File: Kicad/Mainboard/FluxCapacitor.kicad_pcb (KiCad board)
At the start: 2 copper layers, 100 x 100 mm, 99 parts, among them J1 PJ-002A, J2 TM_1, J3 TM_2, J7 TM_4, J8 TM_2, J9 RELAY, M1 SYS_FAN, Q2 IRF4905PBF, Q3 2N7000, Q4 2N7000, U1 OKI-78SR-5_1.5-W36-C, U2 ESP32_DEVBOARD, U4 HT16K33_DEVBOARD, U5 PCA9306DCUR

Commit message: Continued mainboard layout
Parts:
- moved R16 197.6 mm to (274.0, 111.5)
- moved TP23 191.6 mm to (281.5, 24.5)
- moved TP17 188.4 mm to (276.0, 46.5)
- moved C14 188.2 mm to (241.2, 143.0)
- moved C15 188.2 mm to (236.0, 143.3)
- moved C16 188.2 mm to (235.5, 150.5)
- moved C19 188.2 mm to (284.3, 51.9)
- moved C20 188.2 mm to (253.4, 105.5)
- moved C21 188.2 mm to (284.3, 55.0)
- moved C5 188.2 mm to (284.3, 39.9)
- moved C6 188.2 mm to (284.3, 42.9)
- moved C7 188.2 mm to (284.3, 45.9)
- moved D10 188.2 mm to (257.5, 39.9)
- moved D11 188.2 mm to (257.5, 43.0)
- moved D12 188.2 mm to (257.5, 46.0)
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
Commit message: Finished Mainboard Layout
-Now all that needs to be done is to resolve all DRC errors
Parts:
- TP15, TP16, TP17, TP18, TP19, TP20, TP21, TP22, TP23, TP24, TP25, TP6, TP7: footprint FluxCapacitor:TestPoint_Pad_D2.0mm -> FluxCapacitor:TestPoint_Pad_D1.5mm
- moved C19 194.9 mm to (94.0, 94.0), turned to -90 degrees
- moved Q3 186.8 mm to (95.2, 119.2), turned to 90 degrees
- moved TP23 181.5 mm to (121.0, 109.2)
- moved TP3 177.4 mm to (95.5, 61.8), turned to -90 degrees
- moved TP24 174.1 mm to (116.0, 109.2)
- moved R29 170.7 mm to (99.2, 118.0)
- moved R30 170.4 mm to (99.5, 121.0)
- moved TP22 170.1 mm to (123.5, 109.2)
- moved TP21 169.4 mm to (126.0, 109.2)
- moved TP20 168.9 mm to (128.5, 109.2)
- moved TP25 161.1 mm to (133.5, 121.8), turned to 180 degrees
- moved TP19 154.8 mm to (131.0, 109.2)
- moved TP18 154.0 mm to (133.5, 109.2)
- moved C6 152.5 mm to (146.2, 107.5), turned to 180 degrees
- moved C7 132.5 mm to (175.8, 121.8), turned to 180 degrees
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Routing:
- net +3V3: track 0.00 -> 270.6 mm, vias 0 -> 11
- net 5V_RAW: track 0.00 -> 177.3 mm, vias 0 -> 8
- net /I2C_SCL: track 0.00 -> 146.9 mm, vias 0 -> 9
- net /I2C_SDA: track 0.00 -> 143.2 mm, vias 0 -> 8
- net 12V_PROTECTED: track 0.00 -> 134.5 mm, vias 0 -> 10
- net /HALL_1: track 0.00 -> 114.7 mm, vias 0 -> 4
- net /HALL_3: track 0.00 -> 112.2 mm, vias 0 -> 1
- net /HALL_2: track 0.00 -> 101.4 mm
- net Net-(U2-P25): track 0.00 -> 98.8 mm, vias 0 -> 5
- net Net-(U2-P27): track 0.00 -> 89.1 mm, vias 0 -> 1
- net /HALL_4: track 0.00 -> 86.6 mm
- net /12V_RAW: track 0.00 -> 83.0 mm, vias 0 -> 5
- net /M3_PRESET_LED_2: track 0.00 -> 81.3 mm, vias 0 -> 2
- net /BUZZER_DRV: track 0.00 -> 80.9 mm, vias 0 -> 2
- net /MAIN_POWER_SENSE: track 0.00 -> 80.4 mm, vias 0 -> 1
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- added copper zone on B.Cu, net GND
- added copper zone on F.Cu, net GND

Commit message: Finished Mainboard PCB
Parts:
- added REF**: MountingHole_3.2mm_M3, MountingHole:MountingHole_3.2mm_M3, F.Cu at (129.6, 103.2)
- moved TP24 2.30 mm to (118.3, 109.2)
- moved TP6 1.55 mm to (189.1, 55.8), turned to -90 degrees
- moved TP7 1.30 mm to (189.1, 58.3), turned to 180 degrees
- moved R5 1.20 mm to (188.9, 52.6), turned to 90 degrees
- moved D10 0.75 mm to (167.8, 101.5)
- moved D11 0.75 mm to (171.2, 101.5)
- moved D12 0.75 mm to (174.8, 101.5)
- moved D16 0.75 mm to (189.8, 101.5)
- moved D17 0.75 mm to (186.2, 101.5)
- moved D18 0.75 mm to (182.8, 101.5)
- moved D19 0.75 mm to (179.2, 101.5)
- moved D8 0.75 mm to (160.8, 101.5)
- moved D9 0.75 mm to (164.2, 101.5)
- moved R7 0.75 mm to (190.5, 75.0)
- moved R32 0.50 mm to (160.0, 46.8)
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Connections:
- U4 pad 19: /FAULT LEDS/A1 -> unconnected-(U4-A15-Pad19)
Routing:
- net +3V3: track 270.6 -> 289.9 mm, vias 11 -> 15
- net /BTN_EXP_INT: track 75.5 -> 87.5 mm, vias 5 -> 6
- net /I2C_SCL: track 146.9 -> 153.2 mm
- net /12V_RAW: track 83.0 -> 88.7 mm, vias 5 -> 8
- net /FAULT LEDS/A6: track 51.4 -> 57.0 mm, vias 2 -> 5
- net Net-(U2-P27): track 89.1 -> 94.4 mm, vias 1 -> 5
- net Net-(U2-P14): track 71.7 -> 75.4 mm
- net Net-(U2-P26): track 76.7 -> 79.6 mm
- net Net-(U2-P25): track 98.8 -> 101.4 mm, vias 5 -> 7
- net /FAULT LEDS/A1: track 43.4 -> 45.6 mm
- net Net-(D2-K): track 28.6 -> 30.5 mm
- net Net-(U_BTN_EXPANDER1-GPA7): track 2.48 -> 3.76 mm
- net Net-(D9-A): track 2.97 -> 2.22 mm
- net Net-(D8-A): track 2.97 -> 2.22 mm
- net Net-(D19-A): track 2.98 -> 2.23 mm
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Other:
- outline, holes or cut-outs redrawn
- board text added: "12V_PRO"
- board text added: "12V_RAW"
- board text added: "3V3"
- board text added: "5V_RAW"
- board text added: "5V_SYS"
- board text added: "DBG1"
- board text added: "DBG2"
- board text added: "DBG3"
- board text added: "DBG4"
- board text added: "DEBUG LEDS"

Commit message: Added a little mark showing it was my work
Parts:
- added G***: LOGO, FluxCapacitor:FluxCapacitorImage, B.Cu at (175.2, 55.0)
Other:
- board text added: "FLUX CAPACITOR MAINBOARD"
- board text added: "FOR HEELUXE"
- board text added: "MADE BY JOSHUA SMALL"
- board text added: "REV 0 - JULY 2026"

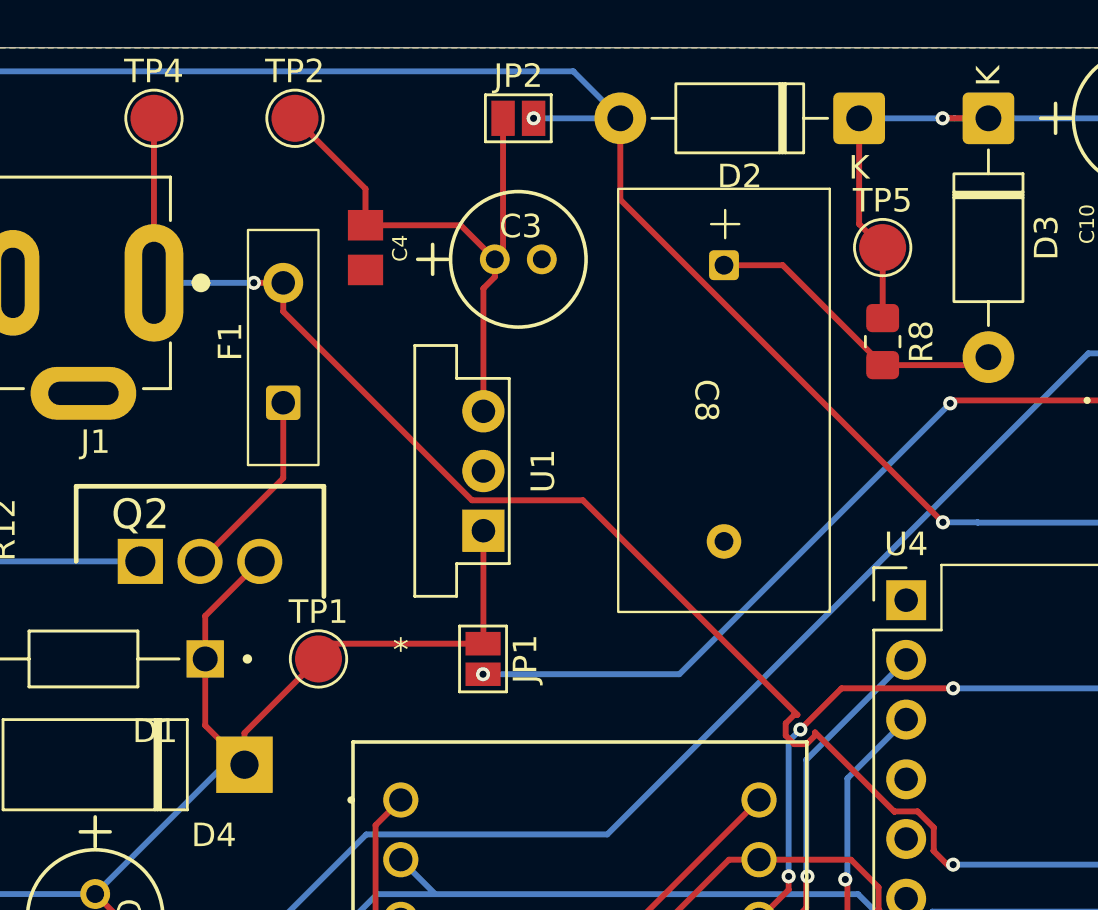
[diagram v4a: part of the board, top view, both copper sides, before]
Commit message: Made relay splitter daughterboard
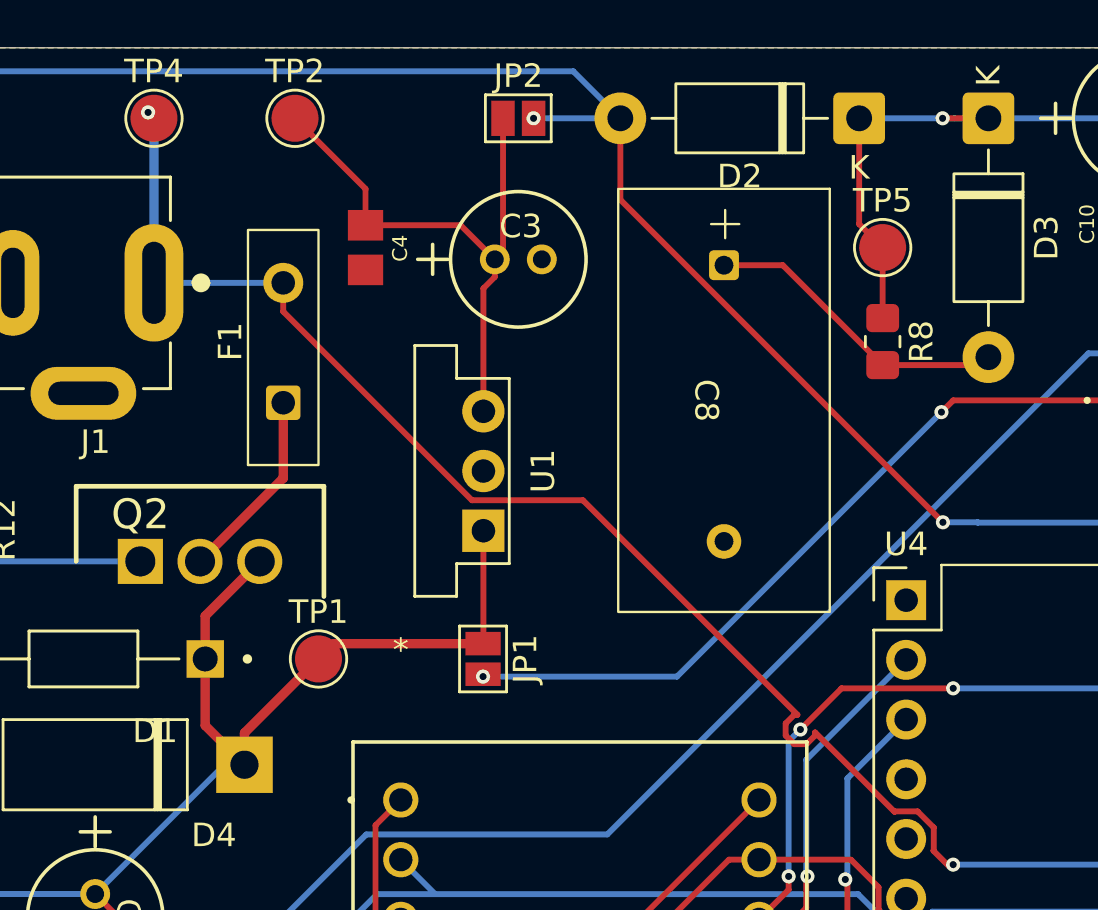
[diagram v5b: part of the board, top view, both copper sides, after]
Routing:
- net /12V_RAW: track 88.7 -> 89.4 mm, vias 8 -> 7
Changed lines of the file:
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@@
 	)
 	(segment
-		(start 112.75 70.75)
-		(end 113.4 70.1)
-		(width 0.25)
+		(start 113.4 70.1)
+		(end 119.75 70.1)
+		(width 0.4)
 		(layer "F.Cu")
 		(net "Net-(D4-K)")
 	)
 	(segment
-		(start 109.6 75.25)
-		(end 109.6 73.9)
+		(start 119.75 70)
+		(end 119.765 69.985)
 		(width 0.25)
 		(layer "F.Cu")
@@
 	)
 	(segment
-		(start 107.93 68.92)
-		(end 110.25 66.6)
+		(start 119.75 70.1)
+		(end 119.75 70)
 		(width 0.25)
 		(layer "F.Cu")
@@
 	)
 	(segment
-		(start 119.75 70)
-		(end 119.765 69.985)
-		(width 0.25)
+		(start 109.6 73.9)
+		(end 112.75 70.75)
+		(width 0.4)
 		(layer "F.Cu")
 		(net "Net-(D4-K)")
 	)
 	(segment
-		(start 119.75 70.1)
-		(end 119.75 70)
-		(width 0.25)
+		(start 107.93 73.58)
+		(end 109.6 75.25)
+		(width 0.4)
 		(layer "F.Cu")
 		(net "Net-(D4-K)")
@@
 	)
 	(segment
-		(start 105.25 82.75)
-		(end 105.25 85.75)
-		(width 0.25)
+		(start 110.25 66.6)
+		(end 107.93 68.92)
+		(width 0.4)
 		(layer "F.Cu")
 		(net "Net-(D4-K)")
 	)
 	(segment
-		(start 107.93 70.75)
-		(end 107.93 68.92)
+		(start 105.25 82.75)
+		(end 105.25 85.75)
 		(width 0.25)
 		(layer "F.Cu")
@@
 	)
 	(segment
-		(start 107.93 73.58)
-		(end 109.6 75.25)
-		(width 0.25)
+		(start 109.6 75.25)
+		(end 109.6 73.9)
+		(width 0.4)
 		(layer "F.Cu")
 		(net "Net-(D4-K)")
 	)
 	(segment
-		(start 109.6 73.9)
-		(end 112.75 70.75)
-		(width 0.25)
+		(start 107.93 68.92)
+		(end 107.93 70.75)
+		(width 0.4)
 		(layer "F.Cu")
 		(net "Net-(D4-K)")
@@
 		(start 107.93 70.75)
 		(end 107.93 73.58)
-		(width 0.25)
+		(width 0.4)
 		(layer "F.Cu")
 		(net "Net-(D4-K)")
 	)
 	(segment
-		(start 113.4 70.1)
-		(end 119.75 70.1)
-		(width 0.25)
+		(start 112.75 70.75)
+		(end 113.4 70.1)
+		(width 0.4)
 		(layer "F.Cu")
 		(net "Net-(D4-K)")
@@
 	)
 	(segment
+		(start 109.6 75.25)
+		(end 108.75 75.25)
+		(width 0.25)
+		(layer "B.Cu")
+		(net "Net-(D4-K)")
+	)
+	(segment
 		(start 108.75 75.25)
 		(end 103.25 80.75)
@@
 	)
 	(segment
-		(start 109.6 75.25)
-		(end 108.75 75.25)
-		(width 0.25)
-		(layer "B.Cu")
-		(net "Net-(D4-K)")
-	)
-	(segment
 		(start 188.25 122.75)
 		(end 188.25 123.805)
@@
 	)
 	(segment
+		(start 139.25 60.25)
+		(end 139.75 59.75)
+		(width 0.25)
+		(layer "F.Cu")
+		(net "12V_PROTECTED")
+	)
+	(segment
 		(start 168.365 112.095991)
 		(end 170.905 114.635991)
@@
 	)
 	(segment
-		(start 139.75 59.75)
-		(end 146.9459 59.75)
-		(width 0.25)
-		(layer "F.Cu")
-		(net "12V_PROTECTED")
-	)
-	(segment
 		(start 167.824476 110.668076)
 		(end 168.365 111.2086)
@@
 	)
 	(segment
-		(start 139.625 59.875)
-		(end 139.75 59.75)
+		(start 139.75 59.75)
+		(end 146.9459 59.75)
 		(width 0.25)
 		(layer "F.Cu")
@@
 	)
 	(via
-		(at 139.625 59.875)
+		(at 139.25 60.25)
 		(size 0.6)
 		(drill 0.3)
@@
 	)
 	(via
-		(at 119.75 71.4)
+		(at 119.75 71.5)
 		(size 0.6)
 		(drill 0.3)
@@
 	)
 	(segment
-		(start 139.625 59.875)
-		(end 128.1 71.4)
-		(width 0.25)
-		(layer "B.Cu")
-		(net "12V_PROTECTED")
-	)
-	(segment
 		(start 165.271092 91.75)
 		(end 165.271092 91.521092)
@@
 	)
 	(segment
-		(start 128.1 71.4)
-		(end 119.75 71.4)
-		(width 0.25)
-		(layer "B.Cu")
-		(net "12V_PROTECTED")
-	)
-	(segment
 		(start 167.824476 110.668076)
 		(end 167.0214 109.865)
@@
 	)
 	(segment
+		(start 139.25 60.25)
+		(end 128 71.5)
+		(width 0.25)
+		(layer "B.Cu")
+		(net "12V_PROTECTED")
+	)
+	(segment
+		(start 128 71.5)
+		(end 119.75 71.5)
+		(width 0.25)
+		(layer "B.Cu")
+		(net "12V_PROTECTED")
+	)
+	(segment
 		(start 180.345 127.9)
 		(end 180.3 127.9)
@@
 	)
 	(segment
+		(start 105.75 47.75)
+		(end 105.5 47.5)
+		(width 0.4)
+		(layer "F.Cu")
+		(net "/12V_RAW")
+	)
+	(segment
 		(start 138.91085 78.91085)
 		(end 139.585 79.585)
@@
 	)
 	(segment
-		(start 105.75 47.75)
-		(end 105.75 54.75)
-		(width 0.25)
-		(layer "F.Cu")
-		(net "/12V_RAW")
-	)
-	(segment
 		(start 137.249149 77.249149)
 		(end 137.263299 77.235)
@@
 	)
 	(segment
-		(start 110 54.75)
-		(end 111.25 54.75)
-		(width 0.25)
-		(layer "F.Cu")
-		(net "/12V_RAW")
-	)
-	(segment
 		(start 139.585 79.585)
 		(end 139.67 79.5)
@@
 	)
 	(via
-		(at 110 54.75)
-		(size 0.6)
-		(drill 0.3)
-		(layers "F.Cu" "B.Cu")
-		(net "/12V_RAW")
-	)
-	(via
 		(at 151.25 92.625)
 		(size 0.6)
@@
 	)
 	(via
-		(at 105.75 54.75)
+		(at 139.75 79.5)
 		(size 0.6)
 		(drill 0.3)
@@
 	)
 	(via
-		(at 139.75 79.5)
+		(at 105.5 47.5)
 		(size 0.6)
 		(drill 0.3)
@@
 	)
 	(segment
+		(start 105.75 54.75)
+		(end 111.25 54.75)
+		(width 0.25)
+		(layer "B.Cu")
+		(net "/12V_RAW")
+	)
+	(segment
+		(start 105.75 47.75)
+		(end 105.75 54.75)
+		(width 0.4)
+		(layer "B.Cu")
+		(net "/12V_RAW")
+	)
+	(segment
 		(start 149.25 86.5)
 		(end 147 86.5)
@@
 	)
 	(segment
-		(start 110 54.75)
-		(end 105.75 54.75)
-		(width 0.25)
+		(start 105.5 47.5)
+		(end 105.75 47.75)
+		(width 0.4)
 		(layer "B.Cu")
 		(net "/12V_RAW")
@@
 	)
 	(segment
-		(start 111.25 63.06)
-		(end 107.71 66.6)
-		(width 0.25)
+		(start 111.25 59.85)
+		(end 111.25 63.06)
+		(width 0.4)
 		(layer "F.Cu")
 		(net "Net-(Q2-D)")
 	)
 	(segment
-		(start 111.25 59.85)
-		(end 111.25 63.06)
-		(width 0.25)
+		(start 111.25 63.06)
+		(end 107.71 66.6)
+		(width 0.4)
 		(layer "F.Cu")
 		(net "Net-(Q2-D)")
